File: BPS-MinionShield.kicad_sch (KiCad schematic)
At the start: 76 parts, among them J1 TempConn1, J2 TempConn2, J3 Conn_01x24_Female

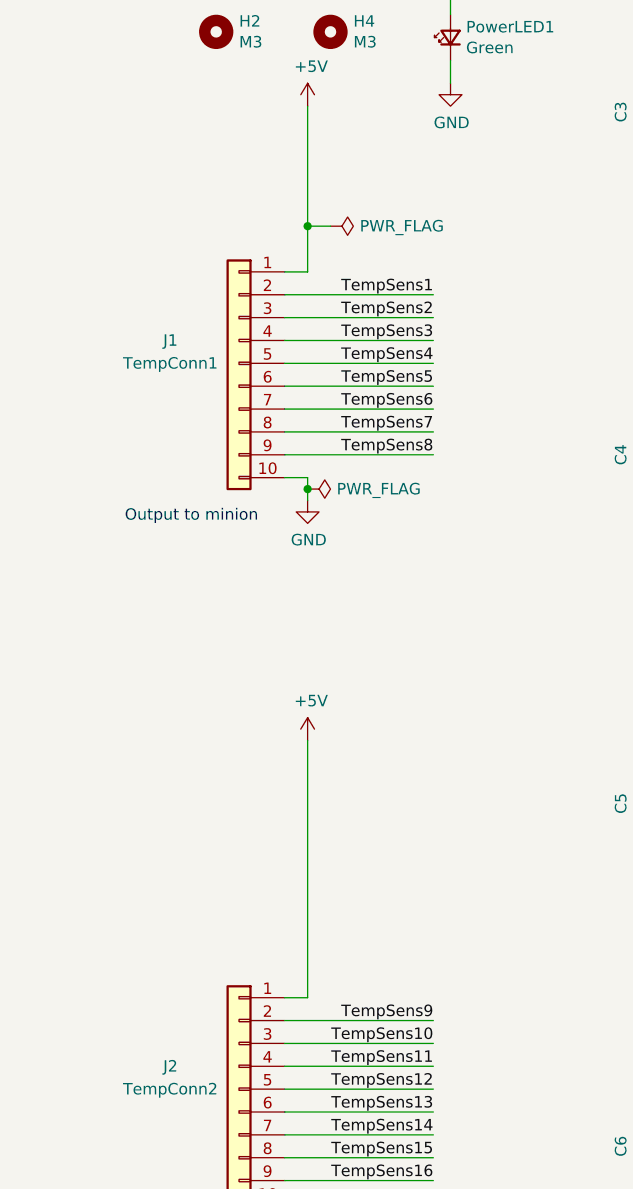
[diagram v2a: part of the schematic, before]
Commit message: Revert "move ferrite beads for more space"
This reverts commit 10398d522d6bd349285b691c333d995223f13479.
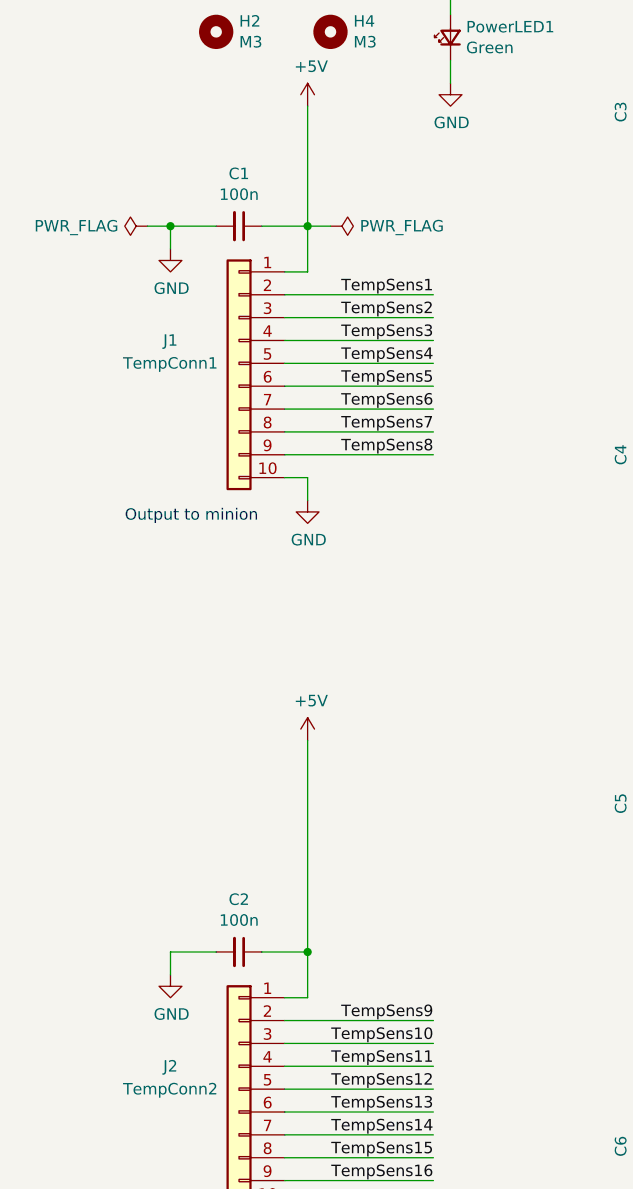
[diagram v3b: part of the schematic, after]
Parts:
- added C1, C2: 100n, Capacitor_SMD:C_0805_2012Metric, symbol Device:C_Small
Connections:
- net +5V: now also C1.1, C2.1
- net GND: now also C1.2, C2.2
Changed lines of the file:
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@@
   (junction (at 164.465 112.395) (diameter 0) (color 0 0 0 0)
   )
-  (junction (at 48.26 82.55) (diameter 0) (color 0 0 0 0)
-  )
   (junction (at 132.715 35.56) (diameter 0) (color 0 0 0 0)
   )
@@
   (junction (at 184.15 35.56) (diameter 0) (color 0 0 0 0)
   )
+  (junction (at 48.26 133.985) (diameter 0) (color 0 0 0 0)
+  )
   (junction (at 88.9 73.66) (diameter 0) (color 0 0 0 0)
   )
@@
   )
   (junction (at 152.4 35.56) (diameter 0) (color 0 0 0 0)
+  )
+  (junction (at 33.02 53.34) (diameter 0) (color 0 0 0 0)
   )
   (junction (at 152.4 150.495) (diameter 0) (color 0 0 0 0)
@@
     (stroke (width 0) (type default) (color 0 0 0 0))
   )
+  (wire (pts (xy 33.02 133.985) (xy 33.02 136.525))
+    (stroke (width 0) (type default) (color 0 0 0 0))
+  )
+  (wire (pts (xy 33.02 53.34) (xy 33.02 55.88))
+    (stroke (width 0) (type default) (color 0 0 0 0))
+  )
   (wire (pts (xy 132.715 150.495) (xy 135.255 150.495))
     (stroke (width 0) (type default) (color 0 0 0 0))
@@
     (stroke (width 0) (type default) (color 0 0 0 0))
   )
+  (wire (pts (xy 30.48 53.34) (xy 33.02 53.34))
+    (stroke (width 0) (type default) (color 0 0 0 0))
+  )
   (wire (pts (xy 88.9 158.115) (xy 88.9 160.655))
     (stroke (width 0) (type default) (color 0 0 0 0))
@@
     (stroke (width 0) (type default) (color 0 0 0 0))
   )
-  (wire (pts (xy 48.26 110.49) (xy 48.26 139.065))
+  (wire (pts (xy 48.26 133.985) (xy 48.26 139.065))
     (stroke (width 0) (type default) (color 0 0 0 0))
   )
@@
     (stroke (width 0) (type default) (color 0 0 0 0))
   )
+  (wire (pts (xy 48.26 53.34) (xy 43.18 53.34))
+    (stroke (width 0) (type default) (color 0 0 0 0))
+  )
   (wire (pts (xy 152.4 73.66) (xy 152.4 76.2))
     (stroke (width 0) (type default) (color 0 0 0 0))
   )
-  (wire (pts (xy 48.26 83.82) (xy 48.26 82.55))
+  (wire (pts (xy 48.26 83.82) (xy 48.26 81.28))
     (stroke (width 0) (type default) (color 0 0 0 0))
   )
@@
     (stroke (width 0) (type default) (color 0 0 0 0))
   )
+  (wire (pts (xy 48.26 133.985) (xy 43.18 133.985))
+    (stroke (width 0) (type default) (color 0 0 0 0))
+  )
   (wire (pts (xy 99.06 73.66) (xy 100.965 73.66))
     (stroke (width 0) (type default) (color 0 0 0 0))
@@
     (stroke (width 0) (type default) (color 0 0 0 0))
   )
+  (wire (pts (xy 48.26 110.49) (xy 48.26 133.985))
+    (stroke (width 0) (type default) (color 0 0 0 0))
+  )
   (wire (pts (xy 203.835 35.56) (xy 207.01 35.56))
     (stroke (width 0) (type default) (color 0 0 0 0))
@@
     (stroke (width 0) (type default) (color 0 0 0 0))
   )
-  (wire (pts (xy 48.26 82.55) (xy 48.26 81.28))
-    (stroke (width 0) (type default) (color 0 0 0 0))
-  )
   (wire (pts (xy 152.4 150.495) (xy 152.4 153.035))
     (stroke (width 0) (type default) (color 0 0 0 0))
@@
     (stroke (width 0) (type default) (color 0 0 0 0))
   )
+  (wire (pts (xy 38.1 133.985) (xy 33.02 133.985))
+    (stroke (width 0) (type default) (color 0 0 0 0))
+  )
   (wire (pts (xy 164.465 35.56) (xy 167.005 35.56))
     (stroke (width 0) (type default) (color 0 0 0 0))
@@
   )
   (wire (pts (xy 88.9 35.56) (xy 88.9 38.1))
+    (stroke (width 0) (type default) (color 0 0 0 0))
+  )
+  (wire (pts (xy 38.1 53.34) (xy 33.02 53.34))
     (stroke (width 0) (type default) (color 0 0 0 0))
   )
@@
     (pin "1")
   )
+  (symbol (lib_id "power:GND") (at 33.02 136.525 0) (unit 1)
+    (in_bom yes) (on_board yes)
+    (property "Reference" "#PWR02" (id 0) (at 33.02 142.875 0)
+      (effects (font (size 1.27 1.27)) hide)
+    )
+    (property "Value" "GND" (id 1) (at 33.147 140.9192 0))
+    (property "Footprint" "" (id 2) (at 33.02 136.525 0)
+      (effects (font (size 1.27 1.27)) hide)
+    )
+    (property "Datasheet" "" (id 3) (at 33.02 136.525 0)
+      (effects (font (size 1.27 1.27)) hide)
+    )
+    (pin "1")
+  )
   (symbol (lib_id "Connector_Generic:Conn_01x10") (at 40.64 68.58 0) (mirror y) (unit 1)
     (in_bom yes) (on_board yes)
@@
     (pin "9")
   )
+  (symbol (lib_id "Device:C_Small") (at 40.64 53.34 270) (unit 1)
+    (in_bom yes) (on_board yes)
+    (property "Reference" "C1" (id 0) (at 40.64 47.5234 90))
+    (property "Value" "100n" (id 1) (at 40.64 49.8348 90))
+    (property "Footprint" "Capacitor_SMD:C_0805_2012Metric" (id 2) (at 40.64 53.34 0)
+      (effects (font (size 1.27 1.27)) hide)
+    )
+    (property "Datasheet" "https://www.mouser.com/ProductDetail/KEMET/C0805C104K5RAC?qs=r%2FVmNO8Tjq4%2F8ymSnGP6Jw%3D%3D" (id 3) (at 40.64 53.34 0)
+      (effects (font (size 1.27 1.27)) hide)
+    )
+    (pin "1")
+    (pin "2")
+  )
+  (symbol (lib_id "power:GND") (at 33.02 55.88 0) (unit 1)
+    (in_bom yes) (on_board yes)
+    (property "Reference" "#PWR01" (id 0) (at 33.02 62.23 0)
+      (effects (font (size 1.27 1.27)) hide)
+    )
+    (property "Value" "GND" (id 1) (at 33.147 60.2742 0))
+    (property "Footprint" "" (id 2) (at 33.02 55.88 0)
+      (effects (font (size 1.27 1.27)) hide)
+    )
+    (property "Datasheet" "" (id 3) (at 33.02 55.88 0)
+      (effects (font (size 1.27 1.27)) hide)
+    )
+    (pin "1")
+  )
   (symbol (lib_id "power:GND") (at 48.26 83.82 0) (unit 1)
     (in_bom yes) (on_board yes)
@@
     (pin "1")
   )
-  (symbol (lib_id "power:PWR_FLAG") (at 48.26 82.55 270) (unit 1)
-    (in_bom yes) (on_board yes)
-    (property "Reference" "#FLG01" (id 0) (at 50.165 82.55 0)
-      (effects (font (size 1.27 1.27)) hide)
-    )
-    (property "Value" "PWR_FLAG" (id 1) (at 51.4858 82.55 90)
+  (symbol (lib_id "power:PWR_FLAG") (at 30.48 53.34 90) (unit 1)
+    (in_bom yes) (on_board yes)
+    (property "Reference" "#FLG01" (id 0) (at 28.575 53.34 0)
+      (effects (font (size 1.27 1.27)) hide)
+    )
+    (property "Value" "PWR_FLAG" (id 1) (at 27.2542 53.34 90)
       (effects (font (size 1.27 1.27)) (justify left))
     )
-    (property "Footprint" "" (id 2) (at 48.26 82.55 0)
-      (effects (font (size 1.27 1.27)) hide)
-    )
-    (property "Datasheet" "~" (id 3) (at 48.26 82.55 0)
+    (property "Footprint" "" (id 2) (at 30.48 53.34 0)
+      (effects (font (size 1.27 1.27)) hide)
+    )
+    (property "Datasheet" "~" (id 3) (at 30.48 53.34 0)
       (effects (font (size 1.27 1.27)) hide)
     )
@@
     (pin "2")
   )
+  (symbol (lib_id "Device:C_Small") (at 40.64 133.985 270) (unit 1)
+    (in_bom yes) (on_board yes)
+    (property "Reference" "C2" (id 0) (at 40.64 128.1684 90))
+    (property "Value" "100n" (id 1) (at 40.64 130.4798 90))
+    (property "Footprint" "Capacitor_SMD:C_0805_2012Metric" (id 2) (at 40.64 133.985 0)
+      (effects (font (size 1.27 1.27)) hide)
+    )
+    (property "Datasheet" "https://www.mouser.com/ProductDetail/KEMET/C0805C104K5RAC?qs=r%2FVmNO8Tjq4%2F8ymSnGP6Jw%3D%3D" (id 3) (at 40.64 133.985 0)
+      (effects (font (size 1.27 1.27)) hide)
+    )
+    (pin "1")
+    (pin "2")
+  )
   (symbol (lib_id "power:GND") (at 152.4 45.72 0) (unit 1)
     (in_bom yes) (on_board yes)
@@
       (reference "#FLG02") (unit 1) (value "PWR_FLAG") (footprint "")
     )
+    (path "/00000000-0000-0000-0000-00005db6d147"
+      (reference "#PWR01") (unit 1) (value "GND") (footprint "")
+    )
+    (path "/00000000-0000-0000-0000-00005db62854"
+      (reference "#PWR02") (unit 1) (value "GND") (footprint "")
+    )
     (path "/00000000-0000-0000-0000-00005db78fe4"
       (reference "#PWR03") (unit 1) (value "+5V") (footprint "")
@@
       (reference "#PWR0101") (unit 1) (value "GND") (footprint "")
     )
+    (path "/00000000-0000-0000-0000-00005db6d140"
+      (reference "C1") (unit 1) (value "100n") (footprint "Capacitor_SMD:C_0805_2012Metric")
+    )
+    (path "/7354a4be-ec88-418b-90fe-a8546f86138b"
+      (reference "C2") (unit 1) (value "100n") (footprint "Capacitor_SMD:C_0805_2012Metric")
+    )
     (path "/0f5e7c1d-b9d8-449c-b2b3-c87304cc4238"

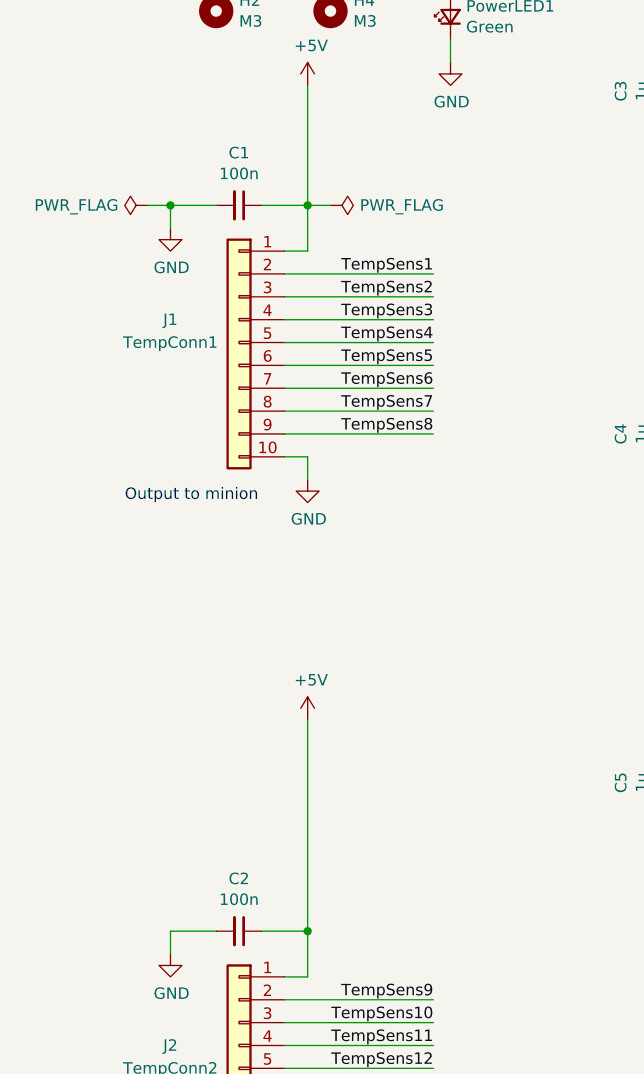
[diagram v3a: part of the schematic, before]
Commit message: fix footprints and reference designators
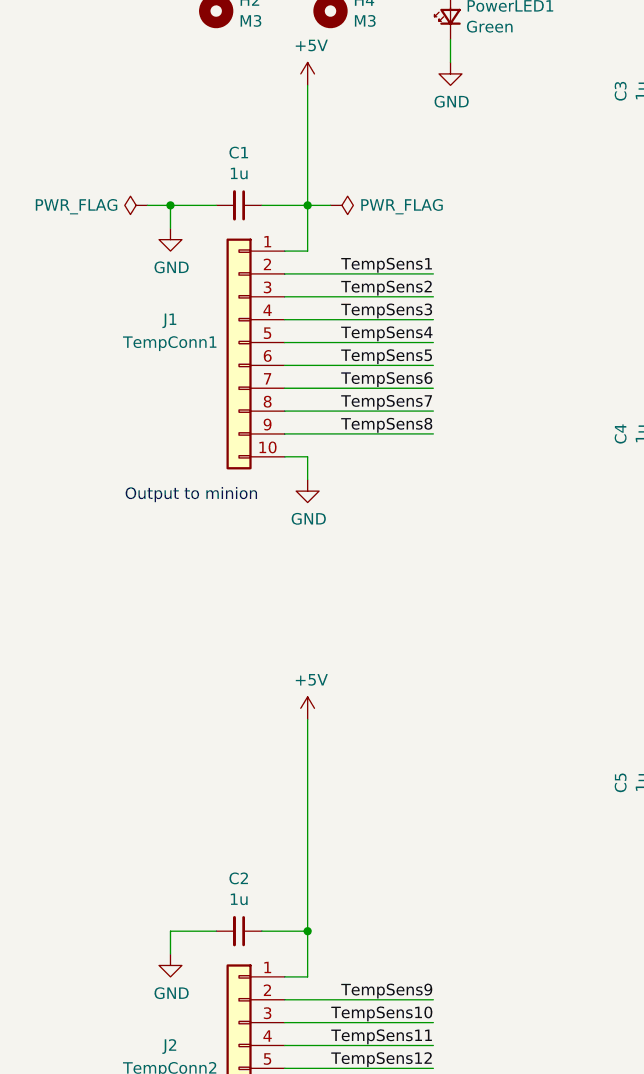
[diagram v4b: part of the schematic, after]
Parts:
- C1, C2: value 100n -> 1u; footprint Capacitor_SMD:C_0805_2012Metric -> Capacitor_SMD:C_0603_1608Metric_Pad1.08x0.95mm_HandSolder
- C10, C11, C12, C13, C14, C15, C16, C17, C18, C3, C4, C5, C6, C7, C8, C9: footprint Capacitor_SMD:C_0805_2012Metric -> Capacitor_SMD:C_0603_1608Metric_Pad1.08x0.95mm_HandSolder
- FB1, FB10, FB11, FB12, FB13, FB14, FB15, FB16, FB17, FB18, FB2, FB3, FB4, FB5, FB6, FB7, FB8, FB9: footprint Inductor_SMD:L_0805_2012Metric -> Inductor_SMD:L_0805_2012Metric_Pad1.05x1.20mm_HandSolder
- PowerLED1: footprint LED_SMD:LED_0805_2012Metric -> LED_SMD:LED_0805_2012Metric_Pad1.15x1.40mm_HandSolder
- R1: footprint Resistor_SMD:R_0805_2012Metric -> Resistor_SMD:R_0805_2012Metric_Pad1.20x1.40mm_HandSolder
- R10, R11, R12, R13, R18, R19, R2, R20, R21, R26, R27, R28, R29, R3, R4, R5: footprint Capacitor_SMD:C_0603_1608Metric -> Resistor_SMD:R_0603_1608Metric_Pad0.98x0.95mm_HandSolder
- R14, R15, R16, R17, R22, R23, R24, R25, R30, R31, R32, R33, R6, R7, R8, R9: footprint Resistor_SMD:R_0603_1608Metric -> Resistor_SMD:R_0603_1608Metric_Pad0.98x0.95mm_HandSolder

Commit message: change to all passives to 0805 footprints
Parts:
- C1, C10, C11, C12, C13, C14, C15, C16, C17, C18, C2, C3, C4, C5, C6, C7, C8, C9: footprint Capacitor_SMD:C_0603_1608Metric_Pad1.08x0.95mm_HandSolder -> Capacitor_SMD:C_0805_2012Metric_Pad1.18x1.45mm_HandSolder
- R10, R11, R12, R13, R14, R15, R16, R17, R18, R19, R2, R20, R21, R22, R23, R24, R25, R26, R27, R28, R29, R3, R30, R31, R32, R33, R4, R5, R6, R7, R8, R9: footprint Resistor_SMD:R_0603_1608Metric_Pad0.98x0.95mm_HandSolder -> Resistor_SMD:R_0805_2012Metric_Pad1.20x1.40mm_HandSolder
